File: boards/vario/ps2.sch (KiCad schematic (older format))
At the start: 58 parts, among them Q3 2N7002, Q4 2N7002, Q5 2N7002, U10 74HC161PW, U11 MC74HC244ADT, U12 74HC74PW, U13 74HC74PW, U14 74HC08PW, U15 74HC74PW, U16 74HC74PW, U17 74HC161PW, U18 74HC273PW, U19 CD74HC280MT, U20 MC74HC151ADTR2G, U21 MC74HC151ADTR2G, U22 MC74HC244ADT, U23 CD74HC280MT, U24 SN74LV10APW, U25 74HC08PW, U26 74HC04PW, U28 SN74HC32PWR, U29 SN74HC32PWR, U30 SN74HC32PWR, U33 74HC08PW, U7 SN74LV14APW, U8 74HC273PW, U9 74HC273PW

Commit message: Vario: power nets
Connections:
- net d0: now also U18.13 (D4); no longer U18.3 (D0)
- net d1: now also U18.14 (D5); no longer U18.4 (D1)
- net d2: now also U18.17 (D6); no longer U18.7 (D2)
- net d3: now also U18.18 (D7); no longer U18.8 (D3)
- net d4: now also U18.3 (D0); no longer U18.13 (D4)
- net d5: now also U18.4 (D1); no longer U18.14 (D5)
- net d6: now also U18.7 (D2); no longer U18.17 (D6)
- net d7: now also U18.8 (D3); no longer U18.18 (D7)
- net send_clk_ena: now also U15.5 (Q); no longer U13.9 (Q)
- net send_clk_ena_clk: now also U15.3 (C); no longer U13.11 (C)
- net send_clk_out: now also U13.8 (~Q); no longer U15.6 (~Q)
- net send_data1: now also U18.12 (Q4); no longer U18.2 (Q0)
- net send_data2: now also U18.15 (Q5); no longer U18.5 (Q1)
- net send_data3: now also U18.16 (Q6); no longer U18.6 (Q2)
- net send_data4: now also U18.19 (Q7); no longer U18.9 (Q3)
- net send_data5: now also U18.2 (Q0); no longer U18.12 (Q4)
- net send_data6: now also U18.5 (Q1); no longer U18.15 (Q5)
- net send_data7: now also U18.6 (Q2); no longer U18.16 (Q6)
- net send_data8: now also U18.9 (Q3); no longer U18.19 (Q7)
- net send_req: now also U13.11 (C); no longer U15.3 (C)
- net ~send_clk_ena: now also U15.6 (~Q); no longer U13.8 (~Q)
- net ~send_clk_out: now also U13.9 (Q); no longer U15.5 (Q)
- net ~send_clk_out_rst: now also U13.13 (~R); no longer U15.1 (~R)
- net ~send_rst: now also U15.1 (~R); no longer U13.13 (~R)
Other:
- moved on the sheet: C19, U13B, U15A, U18
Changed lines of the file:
@@
 L 74xx:74HC74 U13
 U 2 1 5FF12600
-P 10750 8700
-F 0 "U13" H 11100 8500 50  0000 C CNN
-F 1 "74HC74PW" H 11050 8400 50  0000 C CNN
-F 2 "Package_SO:TSSOP-14_4.4x5mm_P0.65mm" H 10750 8700 50  0001 C CNN
-F 3 "http://www.farnell.com/datasheets/1648944.pdf" H 10750 8700 50  0001 C CNN
-	2    10750 8700
+P 7250 8600
+F 0 "U13" H 7600 8400 50  0000 C CNN
+F 1 "74HC74PW" H 7550 8300 50  0000 C CNN
+F 2 "Package_SO:TSSOP-14_4.4x5mm_P0.65mm" H 7250 8600 50  0001 C CNN
+F 3 "http://www.farnell.com/datasheets/1648944.pdf" H 7250 8600 50  0001 C CNN
+	2    7250 8600
 	1    0    0    -1
 $EndComp
@@
 L 74xx:74HC74 U15
 U 1 1 5FF3A4FD
-P 7250 8600
-F 0 "U15" H 7550 8350 50  0000 C CNN
-F 1 "74HC74PW" H 7600 8250 50  0000 C CNN
-F 2 "Package_SO:TSSOP-14_4.4x5mm_P0.65mm" H 7250 8600 50  0001 C CNN
-F 3 "http://www.farnell.com/datasheets/1648944.pdf" H 7250 8600 50  0001 C CNN
-	1    7250 8600
+P 10750 8700
+F 0 "U15" H 11050 8450 50  0000 C CNN
+F 1 "74HC74PW" H 11100 8350 50  0000 C CNN
+F 2 "Package_SO:TSSOP-14_4.4x5mm_P0.65mm" H 10750 8700 50  0001 C CNN
+F 3 "http://www.farnell.com/datasheets/1648944.pdf" H 10750 8700 50  0001 C CNN
+	1    10750 8700
 	1    0    0    -1
 $EndComp
@@
 L 74xx:74HC273 U18
 U 1 1 5FFAC1BC
-P 9800 11900
-F 0 "U18" H 10250 11350 50  0000 C CNN
-F 1 "74HC273PW" H 10300 11250 50  0000 C CNN
-F 2 "Package_SO:TSSOP-20_4.4x6.5mm_P0.65mm" H 9800 11900 50  0001 C CNN
-F 3 "http://www.farnell.com/datasheets/1878567.pdf" H 9800 11900 50  0001 C CNN
-	1    9800 11900
-	1    0    0    -1
-$EndComp
-Wire Wire Line
-	10300 11400 11100 11400
-Wire Wire Line
-	10300 11500 11100 11500
-Wire Wire Line
-	10300 11600 11100 11600
-Wire Wire Line
-	10300 11700 11100 11700
-Wire Wire Line
-	10300 11800 11100 11800
-Wire Wire Line
-	10300 11900 11100 11900
-Wire Wire Line
-	10300 12000 11100 12000
-Wire Wire Line
-	10300 12100 10700 12100
-Wire Wire Line
-	10700 12100 10700 14250
-Wire Wire Line
-	10700 14250 11100 14250
-Text Label 10400 11400 0    50   ~ 0
+P 9600 11900
+F 0 "U18" H 10050 11350 50  0000 C CNN
+F 1 "74HC273PW" H 10100 11250 50  0000 C CNN
+F 2 "Package_SO:TSSOP-20_4.4x6.5mm_P0.65mm" H 9600 11900 50  0001 C CNN
+F 3 "http://www.farnell.com/datasheets/1878567.pdf" H 9600 11900 50  0001 C CNN
+	1    9600 11900
+	1    0    0    -1
+$EndComp
+Text Label 11100 11400 2    50   ~ 0
 send_data1
-Text Label 10400 11500 0    50   ~ 0
+Text Label 11100 11500 2    50   ~ 0
 send_data2
-Text Label 10400 11600 0    50   ~ 0
+Text Label 11100 11600 2    50   ~ 0
 send_data3
-Text Label 10400 11700 0    50   ~ 0
+Text Label 11100 11700 2    50   ~ 0
 send_data4
-Text Label 10400 11800 0    50   ~ 0
-send_data5
-Text Label 10400 11900 0    50   ~ 0
-send_data6
-Text Label 10400 12000 0    50   ~ 0
-send_data7
-Text Label 10700 13250 1    50   ~ 0
+Text Label 11100 14250 2    50   ~ 0
 send_data8
 $Comp
@@
 L power:GND #PWR061
 U 1 1 5FFD0172
-P 9800 12700
-F 0 "#PWR061" H 9800 12450 50  0001 C CNN
-F 1 "GND" H 9805 12527 50  0000 C CNN
-F 2 "" H 9800 12700 50  0001 C CNN
-F 3 "" H 9800 12700 50  0001 C CNN
-	1    9800 12700
+P 9600 12700
+F 0 "#PWR061" H 9600 12450 50  0001 C CNN
+F 1 "GND" H 9605 12527 50  0000 C CNN
+F 2 "" H 9600 12700 50  0001 C CNN
+F 3 "" H 9600 12700 50  0001 C CNN
+	1    9600 12700
 	1    0    0    -1
 $EndComp
@@
 L power:VCC #PWR060
 U 1 1 5FFD069A
-P 9800 11100
-F 0 "#PWR060" H 9800 10950 50  0001 C CNN
-F 1 "VCC" H 9815 11273 50  0000 C CNN
-F 2 "" H 9800 11100 50  0001 C CNN
-F 3 "" H 9800 11100 50  0001 C CNN
-	1    9800 11100
-	1    0    0    -1
-$EndComp
-Text Label 9300 11400 2    50   ~ 0
+P 9600 11100
+F 0 "#PWR060" H 9600 10950 50  0001 C CNN
+F 1 "VCC" H 9615 11273 50  0000 C CNN
+F 2 "" H 9600 11100 50  0001 C CNN
+F 3 "" H 9600 11100 50  0001 C CNN
+	1    9600 11100
+	1    0    0    -1
+$EndComp
+Text Label 9100 11800 2    50   ~ 0
 d0
-Text Label 9300 11500 2    50   ~ 0
+Text Label 9100 11900 2    50   ~ 0
 d1
-Text Label 9300 11600 2    50   ~ 0
+Text Label 9100 12000 2    50   ~ 0
 d2
-Text Label 9300 11700 2    50   ~ 0
+Text Label 9100 12100 2    50   ~ 0
 d3
-Text Label 9300 11800 2    50   ~ 0
+Text Label 9100 11400 2    50   ~ 0
 d4
-Text Label 9300 11900 2    50   ~ 0
+Text Label 9100 11500 2    50   ~ 0
 d5
-Text Label 9300 12000 2    50   ~ 0
+Text Label 9100 11600 2    50   ~ 0
 d6
-Text Label 9300 12100 2    50   ~ 0
+Text Label 9100 11700 2    50   ~ 0
 d7
-Text Label 9300 12400 2    50   ~ 0
+Text Label 9100 12400 2    50   ~ 0
 ~rst
-Text Label 9300 12300 2    50   ~ 0
+Text Label 9100 12300 2    50   ~ 0
 send_ena_clk
 $Comp
@@
 L Device:C C19
 U 1 1 60447330
-P 9400 10900
-F 0 "C19" H 9515 10946 50  0000 L CNN
-F 1 "0.1" H 9515 10855 50  0000 L CNN
-F 2 "Capacitor_SMD:C_0805_2012Metric" H 9438 10750 50  0001 C CNN
-F 3 "~" H 9400 10900 50  0001 C CNN
-	1    9400 10900
+P 9200 10900
+F 0 "C19" H 9315 10946 50  0000 L CNN
+F 1 "0.1" H 9315 10855 50  0000 L CNN
+F 2 "Capacitor_SMD:C_0805_2012Metric" H 9238 10750 50  0001 C CNN
+F 3 "~" H 9200 10900 50  0001 C CNN
+	1    9200 10900
 	1    0    0    -1
 $EndComp
@@
 L power:GND #PWR0131
 U 1 1 60447336
-P 9400 11050
-F 0 "#PWR0131" H 9400 10800 50  0001 C CNN
-F 1 "GND" H 9405 10877 50  0000 C CNN
-F 2 "" H 9400 11050 50  0001 C CNN
-F 3 "" H 9400 11050 50  0001 C CNN
-	1    9400 11050
+P 9200 11050
+F 0 "#PWR0131" H 9200 10800 50  0001 C CNN
+F 1 "GND" H 9205 10877 50  0000 C CNN
+F 2 "" H 9200 11050 50  0001 C CNN
+F 3 "" H 9200 11050 50  0001 C CNN
+	1    9200 11050
 	1    0    0    -1
 $EndComp
@@
 L power:VCC #PWR0130
 U 1 1 6044733C
-P 9400 10750
-F 0 "#PWR0130" H 9400 10600 50  0001 C CNN
-F 1 "VCC" H 9415 10923 50  0000 C CNN
-F 2 "" H 9400 10750 50  0001 C CNN
-F 3 "" H 9400 10750 50  0001 C CNN
-	1    9400 10750
+P 9200 10750
+F 0 "#PWR0130" H 9200 10600 50  0001 C CNN
+F 1 "VCC" H 9215 10923 50  0000 C CNN
+F 2 "" H 9200 10750 50  0001 C CNN
+F 3 "" H 9200 10750 50  0001 C CNN
+	1    9200 10750
 	1    0    0    -1
 $EndComp
@@
 Wire Wire Line
 	6750 5450 6750 5150
+Text Label 10100 11800 0    50   ~ 0
+send_data1
+Text Label 10100 11900 0    50   ~ 0
+send_data2
+Text Label 10100 12000 0    50   ~ 0
+send_data3
+Text Label 10100 12100 0    50   ~ 0
+send_data4
+Text Label 11100 12000 2    50   ~ 0
+send_data7
+Text Label 11100 11900 2    50   ~ 0
+send_data6
+Text Label 11100 11800 2    50   ~ 0
+send_data5
+Text Label 10100 11600 0    50   ~ 0
+send_data7
+Text Label 10100 11500 0    50   ~ 0
+send_data6
+Text Label 10100 11400 0    50   ~ 0
+send_data5
 Wire Bus Line
 	1550 2200 1550 3200
+Text Label 10100 11700 0    50   ~ 0
+send_data8
 $EndSCHEMATC

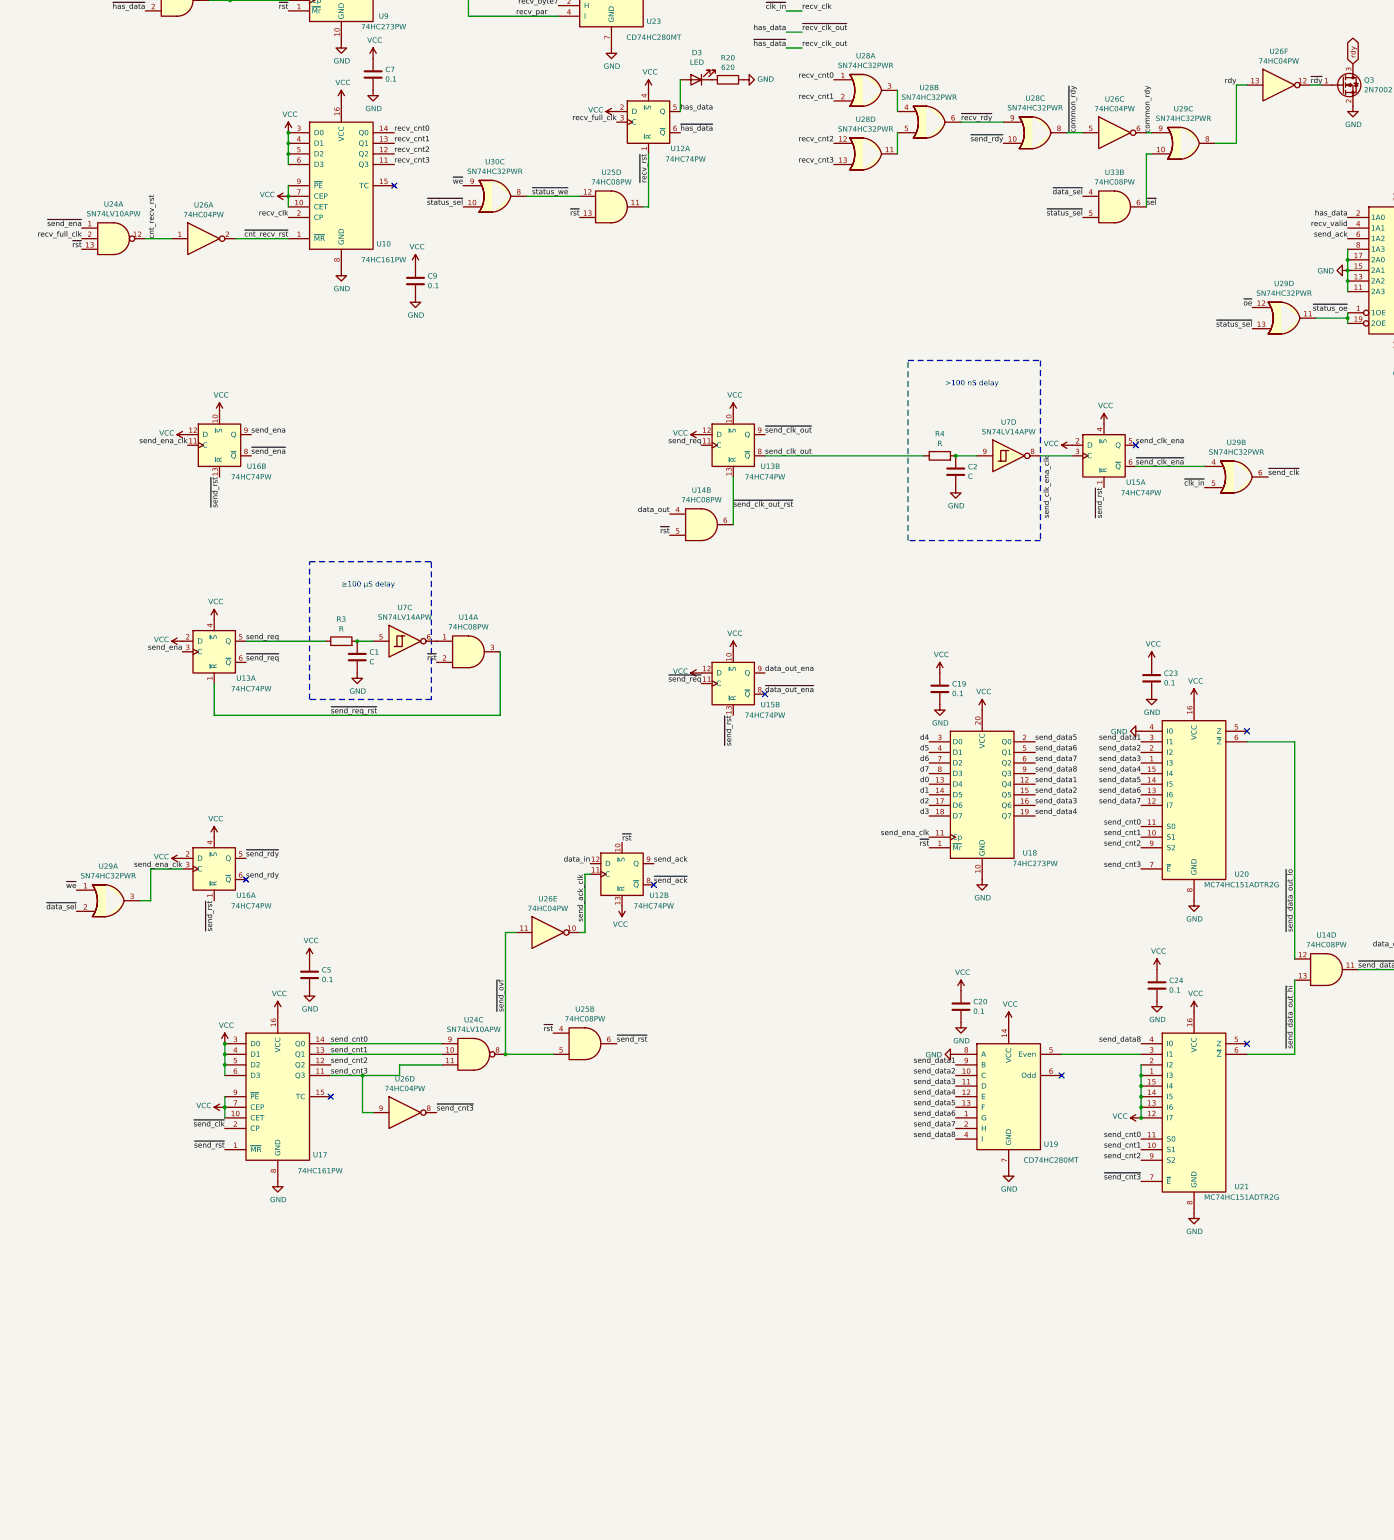
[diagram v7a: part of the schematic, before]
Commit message: Vario: board, delete redundant 7474
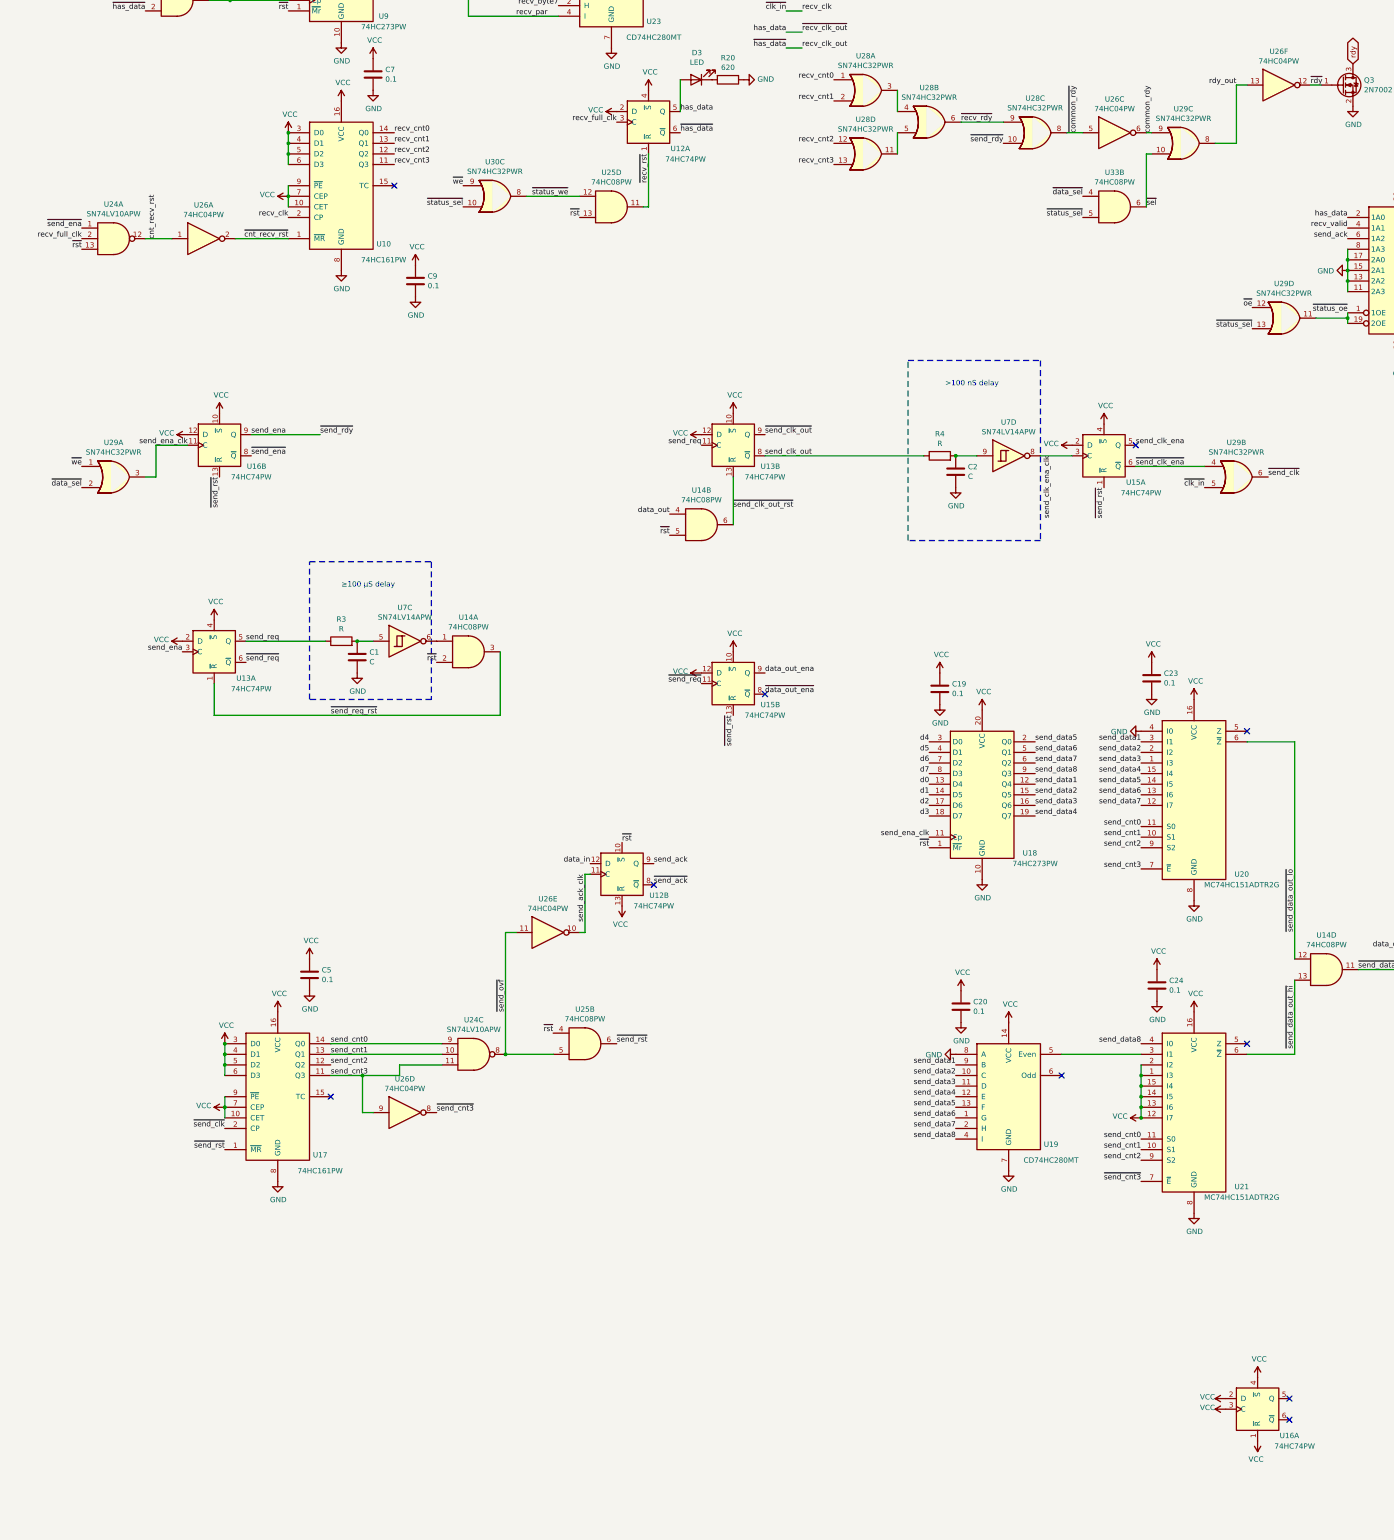
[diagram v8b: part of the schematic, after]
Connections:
- net VCC: now also U16.1 (~R), U16.3 (C)
- net rdy: no longer U26.13, U29.8
- net send_ena: now also U28.10
- net send_ena_clk: no longer U16.3 (C)
- net ~send_rst: no longer U16.1 (~R)
- net send_rdy: no longer names the net of U16.6 (~Q)
- net ~send_rdy: no longer names the net of U16.5 (Q)
- net ~send_rdy: no longer U28.10
- new net rdy_out: U26.13, U29.8
- no-connect marks 17 -> 18
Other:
- moved on the sheet: U16A, U29A
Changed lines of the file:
@@
 Text Label 2400 8900 3    50   ~ 0
 ~send_rst
-Text Label 2100 8600 2    50   ~ 0
-send_ena_clk
 $Comp
 L 74xx:74HC74 U13
@@
 L 74xx:74HC74 U16
 U 1 1 5FF6A7CF
-P 2350 12600
-F 0 "U16" H 2650 12350 50  0000 C CNN
-F 1 "74HC74PW" H 2700 12250 50  0000 C CNN
-F 2 "Package_SO:TSSOP-14_4.4x5mm_P0.65mm" H 2350 12600 50  0001 C CNN
-F 3 "http://www.farnell.com/datasheets/1648944.pdf" H 2350 12600 50  0001 C CNN
-	1    2350 12600
+P 12200 17700
+F 0 "U16" H 12500 17450 50  0000 C CNN
+F 1 "74HC74PW" H 12550 17350 50  0000 C CNN
+F 2 "Package_SO:TSSOP-14_4.4x5mm_P0.65mm" H 12200 17700 50  0001 C CNN
+F 3 "http://www.farnell.com/datasheets/1648944.pdf" H 12200 17700 50  0001 C CNN
+	1    12200 17700
 	1    0    0    -1
 $EndComp
@@
 	1    0    0    -1
 $EndComp
-Text Label 2650 12500 0    50   ~ 0
+Text Label 3350 8500 0    50   ~ 0
 ~send_rdy
-Text Label 2650 12700 0    50   ~ 0
-send_rdy
-$Comp
-L power:VCC #PWR052
-U 1 1 5FF6FC6B
-P 2050 12500
-F 0 "#PWR052" H 2050 12350 50  0001 C CNN
-F 1 "VCC" V 2065 12627 50  0000 L CNN
-F 2 "" H 2050 12500 50  0001 C CNN
-F 3 "" H 2050 12500 50  0001 C CNN
-	1    2050 12500
-	0    -1   -1   0
-$EndComp
-$Comp
-L power:VCC #PWR053
-U 1 1 5FF70430
-P 2350 12300
-F 0 "#PWR053" H 2350 12150 50  0001 C CNN
-F 1 "VCC" H 2365 12473 50  0000 C CNN
-F 2 "" H 2350 12300 50  0001 C CNN
-F 3 "" H 2350 12300 50  0001 C CNN
-	1    2350 12300
-	1    0    0    -1
-$EndComp
-Text Label 2050 12600 2    50   ~ 0
+Text Label 2100 8600 2    50   ~ 0
 send_ena_clk
-Text Label 2350 12900 3    50   ~ 0
-~send_rst
 Text Label 6500 12550 0    50   ~ 0
 send_ack
@@
 L 74xx:74LS32 U29
 U 1 1 60233636
-P 1350 12900
-F 0 "U29" H 1350 13225 50  0000 C CNN
-F 1 "SN74HC32PWR" H 1350 13134 50  0000 C CNN
-F 2 "Package_SO:TSSOP-14_4.4x5mm_P0.65mm" H 1350 12900 50  0001 C CNN
-F 3 "http://www.farnell.com/datasheets/1648978.pdf" H 1350 12900 50  0001 C CNN
-	1    1350 12900
+P 1400 8900
+F 0 "U29" H 1400 9225 50  0000 C CNN
+F 1 "SN74HC32PWR" H 1400 9134 50  0000 C CNN
+F 2 "Package_SO:TSSOP-14_4.4x5mm_P0.65mm" H 1400 8900 50  0001 C CNN
+F 3 "http://www.farnell.com/datasheets/1648978.pdf" H 1400 8900 50  0001 C CNN
+	1    1400 8900
 	1    0    0    -1
 $EndComp
@@
 $EndComp
 Wire Wire Line
-	1650 12900 1750 12900
-Wire Wire Line
-	1750 12900 1750 12600
-Wire Wire Line
-	1750 12600 2050 12600
-Text Label 1050 13000 2    50   ~ 0
+	1700 8900 1800 8900
+Wire Wire Line
+	1800 8900 1800 8600
+Wire Wire Line
+	1800 8600 2100 8600
+Text Label 1100 9000 2    50   ~ 0
 ~data_sel
-Text Label 1050 12800 2    50   ~ 0
+Text Label 1100 8800 2    50   ~ 0
 ~we
 Wire Wire Line
@@
 	12000 5200 12100 5200
 Text Label 12000 5200 2    50   ~ 0
-rdy
+rdy_out
 Wire Wire Line
 	12750 7400 13050 7400
@@
 	1    0    0    -1
 $EndComp
-NoConn ~ 2650 12700
 NoConn ~ 7550 10950
 NoConn ~ 11050 8600
@@
 Text Label 10100 11400 0    50   ~ 0
 send_data5
+Text Label 10100 11700 0    50   ~ 0
+send_data8
+Wire Wire Line
+	3350 8500 2700 8500
+$Comp
+L power:VCC #PWR0231
+U 1 1 605CEC26
+P 11900 17600
+F 0 "#PWR0231" H 11900 17450 50  0001 C CNN
+F 1 "VCC" V 11915 17773 50  0000 C CNN
+F 2 "" H 11900 17600 50  0001 C CNN
+F 3 "" H 11900 17600 50  0001 C CNN
+	1    11900 17600
+	0    -1   -1   0
+$EndComp
+$Comp
+L power:VCC #PWR0232
+U 1 1 605CF77E
+P 11900 17700
+F 0 "#PWR0232" H 11900 17550 50  0001 C CNN
+F 1 "VCC" V 11915 17873 50  0000 C CNN
+F 2 "" H 11900 17700 50  0001 C CNN
+F 3 "" H 11900 17700 50  0001 C CNN
+	1    11900 17700
+	0    -1   -1   0
+$EndComp
+$Comp
+L power:VCC #PWR0233
+U 1 1 605CFAA7
+P 12200 17400
+F 0 "#PWR0233" H 12200 17250 50  0001 C CNN
+F 1 "VCC" H 12215 17573 50  0000 C CNN
+F 2 "" H 12200 17400 50  0001 C CNN
+F 3 "" H 12200 17400 50  0001 C CNN
+	1    12200 17400
+	1    0    0    -1
+$EndComp
+$Comp
+L power:VCC #PWR0234
+U 1 1 605D02A4
+P 12200 18000
+F 0 "#PWR0234" H 12200 17850 50  0001 C CNN
+F 1 "VCC" H 12215 18173 50  0000 C CNN
+F 2 "" H 12200 18000 50  0001 C CNN
+F 3 "" H 12200 18000 50  0001 C CNN
+	1    12200 18000
+	-1   0    0    1
+$EndComp
+NoConn ~ 12500 17600
+NoConn ~ 12500 17800
 Wire Bus Line
 	1550 2200 1550 3200
-Text Label 10100 11700 0    50   ~ 0
-send_data8
 $EndSCHEMATC
